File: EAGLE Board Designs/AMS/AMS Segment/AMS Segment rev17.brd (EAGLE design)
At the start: 275.2 x 86 mm, 338 parts, among them J1 CONNECTOR-2_MICROFIT_SMD_RIGH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, J10 CONNECTOR-2_MICROFIT_SMD_RIGH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, J100 CONNECTOR-1_5222_, J101 CONNECTOR-1_5222_, J102 CONNECTOR-1_5222_, J103 CONNECTOR-1_5222_, J104 CONNECTOR-1_5222_, J105 CONNECTOR-1_5222_, J106 CONNECTOR-1_5222_, J107 CONNECTOR-1_5222_, J108 CONNECTOR-1_5222_, J109 CONNECTOR-1_5222_, J110 CONNECTOR-1_5222_, J111 CONNECTOR-1_5222_, J112 CONNECTOR-1_5222_, J113 CONNECTOR-1_5222_, J114 CONNECTOR-1_5222_, J115 CONNECTOR-1_5222_, J116 CONNECTOR-1_5222_, J117 CONNECTOR-1_5222_, J118 CONNECTOR-1_5222_, J119 CONNECTOR-1_5222_, J120 CONNECTOR-1_5222_, J121 CONNECTOR-1_5222_, J2 CONNECTOR-2_MICROFIT_SMD_RIGH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, J3 CONNECTOR-2_MICROFIT_SMD_RIGH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, J4 CONNECTOR-2_MICROFIT_SMD_RIGH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, J5 CONNECTOR-2_MICROFIT_SMD_RIGH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, J6 CONNECTOR-2_MICROFIT_SMD_RIGH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, J7 CONNECTOR-2_MICROFIT_SMD_RIGH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, J8 CONNECTOR-2_MICROFIT_SMD_RIGH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, J9 CONNECTOR-2_MICROFIT_SMD_RIGH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, T1 TRANSFORMER_HM2112ZNLT, U1 LTC6811-2, U2 LTC6811-2, U3 SHT31-ARP-B, U4 SHT31-ARP-B, U5 LT3990-5, U6 LT3990-5

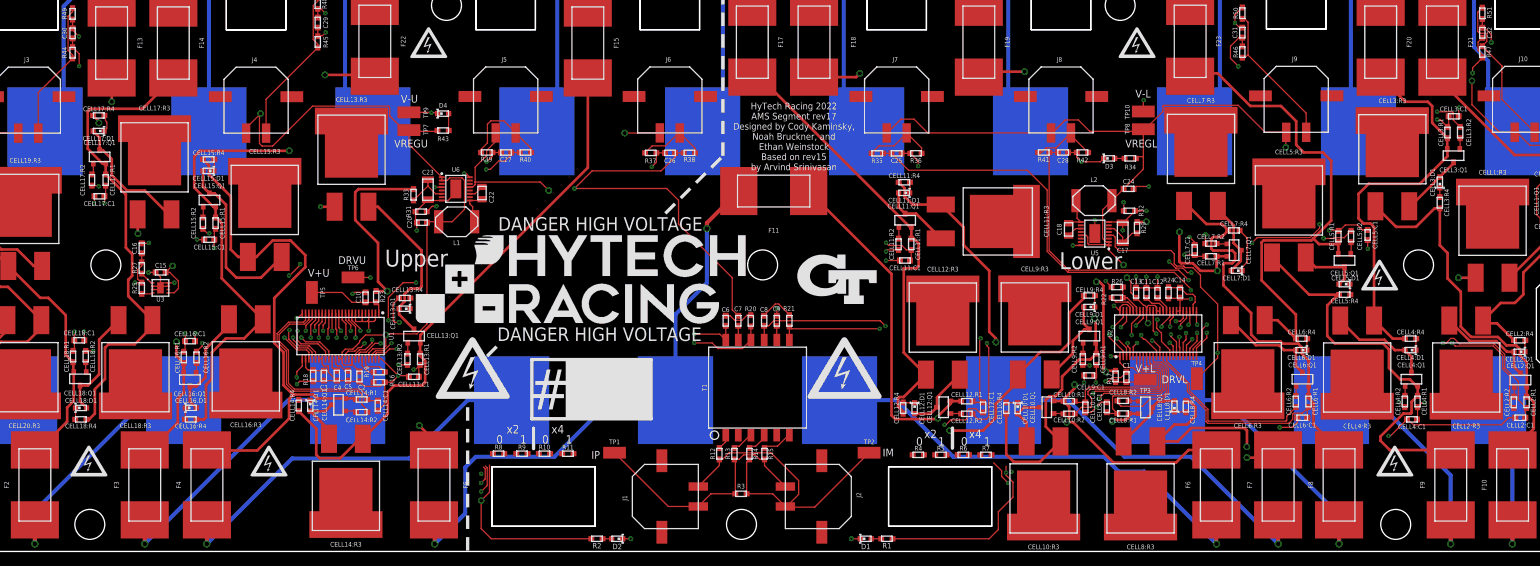
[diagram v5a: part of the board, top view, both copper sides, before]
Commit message: Passes drc and erc
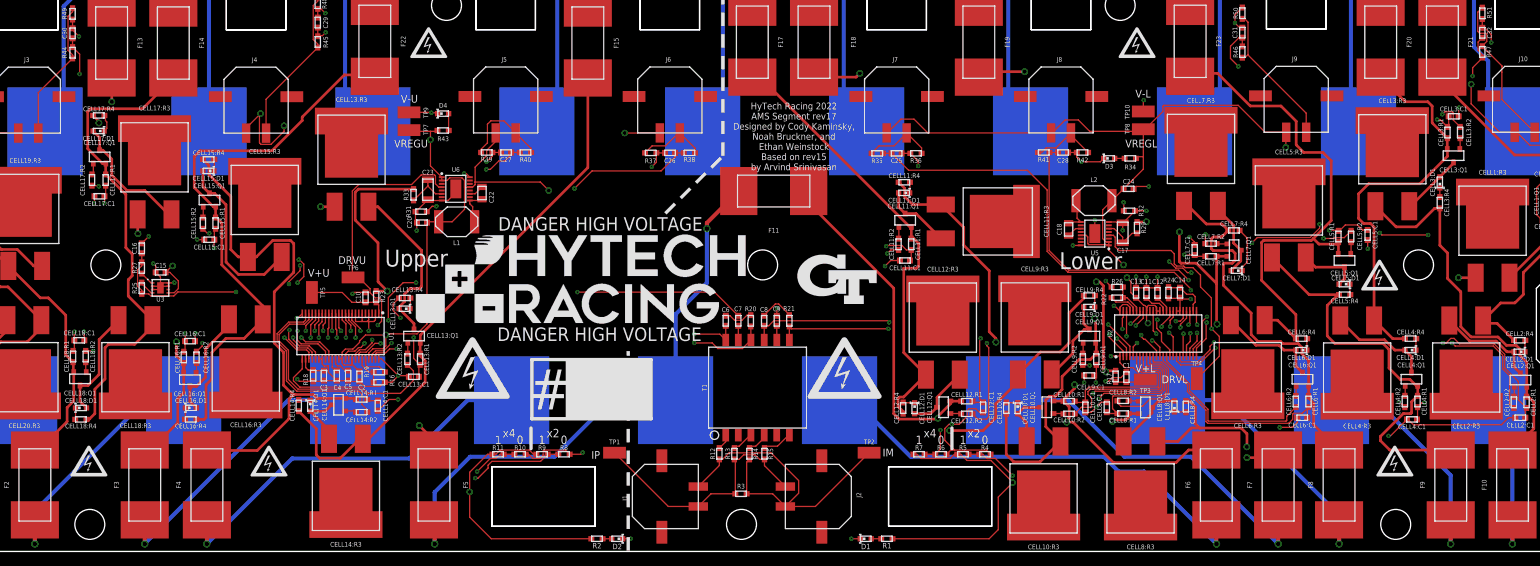
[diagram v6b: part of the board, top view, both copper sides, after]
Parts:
- moved R11 10.5 mm to (100.3, -71.4)
- moved R7 10.1 mm to (163.6, -71.4)
- moved R4 10.0 mm to (173.5, -71.4)
- moved R8 9.83 mm to (110.2, -71.4)
- moved R10 3.68 mm to (103.6, -71.4)
- moved R6 3.37 mm to (166.9, -71.4)
- moved R5 3.32 mm to (170.2, -71.4)
- moved R9 3.02 mm to (106.9, -71.4)
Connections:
- net GPIO5U: now also R25.2; no longer R25.1
- net N$25: now also R8.1; no longer R8.2
- net N$30: now also R25.1; no longer R25.2
- net N$54: now also R10.1; no longer R10.2
- net N$67: now also R4.1, R5.2; no longer R4.2, R5.1
- net N$68: now also R6.1; no longer R6.2
- net V-L: now also R4.2, R6.2; no longer R4.1, R6.1
- net V-U: now also R10.2, R8.2; no longer R10.1, R8.1
- net VREGL: now also R5.1; no longer R5.2
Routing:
- net SENSE7: track 160.0 -> 107.5 mm
- net S3L: track 117.6 -> 66.6 mm
- net S1U: track 72.0 -> 26.2 mm, vias 2 -> 0
- net C3L: track 113.4 -> 67.6 mm
- net GPIO2U: track 85.5 -> 59.9 mm, vias 2 -> 4
- net DRVU: track 71.2 -> 46.8 mm, vias 3 -> 2
- net N$68: track 35.1 -> 53.8 mm
- net C1L: track 93.4 -> 74.8 mm
- net GPIO5U: track 58.3 -> 40.7 mm
- net C2L: track 78.8 -> 64.8 mm
- net S1L: track 83.4 -> 69.7 mm
- net V-L: track 126.7 -> 138.2 mm
- net C11L: track 62.9 -> 51.6 mm
- net S2L: track 73.5 -> 62.2 mm
- net N$25: track 36.2 -> 45.6 mm
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
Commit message: Renumbered
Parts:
- C1: value CAPACITOR_0603_100V_0.1UF -> CAPACITOR_0603_10V_0.1UF
- C11: value CAPACITOR_0603_10V_1UF -> CAPACITOR_1206_100V_2.2UF; device HyTechDevices:0603-CAP -> HyTechDevices:1206-CAP
- C12: value CAPACITOR_0603_10V_1UF -> CAPACITOR_0805_100V_0.22UF; device HyTechDevices:0603-CAP -> HyTechDevices:0805-CAP
- C13, C20, C4, C5: value CAPACITOR_0603_10V_1UF -> CAPACITOR_0603_100V_10NF
- C15: value CAPACITOR_0603_10V_0.1UF -> CAPACITOR_0603_10V_10NF
- C16: value CAPACITOR_0603_10V_3.3NF -> CAPACITOR_0603_10V_15PF
- C17: value CAPACITOR_1206_100V_2.2UF -> CAPACITOR_0603_10V_10NF; device HyTechDevices:1206-CAP -> HyTechDevices:0603-CAP
- C18: value CAPACITOR_0805_100V_0.22UF -> CAPACITOR_0603_10V_15PF; device HyTechDevices:0805-CAP -> HyTechDevices:0603-CAP
- C19: value CAPACITOR_0603_10V_0.1UF -> CAPACITOR_0603_100V_10NF
- C2: value CAPACITOR_0603_10V_22UF -> CAPACITOR_0603_10V_3.3NF
- C21: value CAPACITOR_0603_10V_3.3NF -> CAPACITOR_0805_100V_0.22UF; device HyTechDevices:0603-CAP -> HyTechDevices:0805-CAP
- C22: value CAPACITOR_0805_100V_0.22UF -> CAPACITOR_1206_100V_2.2UF; device HyTechDevices:0805-CAP -> HyTechDevices:1206-CAP
- C23: value CAPACITOR_1206_100V_2.2UF -> CAPACITOR_0603_10V_1UF; device HyTechDevices:1206-CAP -> HyTechDevices:0603-CAP
- C24: value CAPACITOR_0603_10V_22UF -> CAPACITOR_0603_100V_0.1UF
- C25: value CAPACITOR_0603_100V_10NF -> CAPACITOR_0603_10V_22UF
- C26, C27: value CAPACITOR_0603_100V_10NF -> CAPACITOR_0603_10V_1UF
- C30: value CAPACITOR_0603_100V_10NF -> CAPACITOR_0603_10V_0.1UF
- C31: value CAPACITOR_0603_100V_10NF -> CAPACITOR_0603_10V_3.3NF
- C6, C8: value CAPACITOR_0603_10V_15PF -> CAPACITOR_0603_10V_1UF
- C7: value CAPACITOR_0603_10V_10NF -> CAPACITOR_0603_10V_1UF
- C9: value CAPACITOR_0603_10V_10NF -> CAPACITOR_0603_10V_22UF
- R1, R22: value RESISTOR_0603_1K -> RESISTOR_0603_100
- R10: value RESISTOR_0603_DNP -> RESISTOR_0603_374K
- R11, R9: value RESISTOR_0603_DNP -> RESISTOR_0603_1K
- R12: value RESISTOR_0603_22 -> RESISTOR_0603_1K
- R13, R15: value RESISTOR_0603_22 -> RESISTOR_0603_100
- R14: value RESISTOR_0603_22 -> RESISTOR_0603_2.74K
- R16, R19, R2, R34: value RESISTOR_0603_1K -> RESISTOR_0603_DNP
- R17, R18, R37: value RESISTOR_0603_100 -> RESISTOR_0603_DNP
- R20: value RESISTOR_0603_402 -> RESISTOR_0603_2.74K
- R21: value RESISTOR_0603_402 -> RESISTOR_0603_1K
- R23, R25: value RESISTOR_0603_100 -> RESISTOR_0603_402
- R24: value RESISTOR_0603_100 -> RESISTOR_0603_22
- R26: value RESISTOR_0603_1K -> RESISTOR_0603_22
- R28: value RESISTOR_0603_DNP -> RESISTOR_0603_22
- R29: value RESISTOR_0603_470 -> RESISTOR_0603_22
- R3, R5: value RESISTOR_0603_DNP -> RESISTOR_0603_2.74K
- R30, R45: value RESISTOR_0603_100 -> RESISTOR_0603_2.74K
- R31: value RESISTOR_0603_374K -> RESISTOR_0603_100
- R32: value RESISTOR_0603_374K -> RESISTOR_0603_1K
- R33: value RESISTOR_0603_470 -> RESISTOR_0603_DNP
- R36, R48: value RESISTOR_0603_2.74K -> RESISTOR_0603_DNP
- R39, R42: value RESISTOR_0603_2.74K -> RESISTOR_0603_1K
- R4, R6, R7: value RESISTOR_0603_DNP -> RESISTOR_0603_100
- R40: value RESISTOR_0603_100 -> RESISTOR_0603_374K
- R41: value RESISTOR_0603_100 -> RESISTOR_0603_470
- R49, R51: value RESISTOR_0603_2.74K -> RESISTOR_0603_100
- R8: value RESISTOR_0603_DNP -> RESISTOR_0603_470
- U$1, U$23, U$25: device HyTechDevices:MOUNTING_M4 -> HyTechAesthetics:HV_0.50"
- U$10: device HyTechAesthetics:DANGER_HIGH_VOLTAGE -> HyTechAesthetics:LOGO_GT_MEDIUM
- U$100, U$104: device HyTechAesthetics:HV_LARGE -> HyTechAesthetics:HV_0.50"
- U$102, U$103: device HyTechAesthetics:HV_0.50" -> HyTechAesthetics:HV_LARGE
- U$11: device HyTechAesthetics:LOGO_HYTECH_LARGE -> HyTechDevices:MOUNTING_M4
- U$12: device HyTechAesthetics:LOGO_GT_MEDIUM -> HyTechDevices:MOUNTING_M4
- U$13: device HyTechAesthetics:HV_0.50" -> HyTechAesthetics:DANGER_HIGH_VOLTAGE
- U$14: device HyTechDevices:MOUNTING_M4 -> HyTechAesthetics:DANGER_HIGH_VOLTAGE
- U$15: device HyTechDevices:MOUNTING_M4 -> HyTechAesthetics:NUMBER
- U$16: device HyTechDevices:MOUNTING_M4 -> HyTechAesthetics:HV_1.00"
- U$17: device HyTechAesthetics:DANGER_HIGH_VOLTAGE -> HyTechDevices:MOUNTING_M4
- U$19: device HyTechAesthetics:HV_0.50" -> HyTechAesthetics:LOGO_HYTECH_LARGE
- U$21, U$4: device HyTechAesthetics:HV_0.50" -> HyTechDevices:MOUNTING_M4
- U$7: device HyTechAesthetics:NUMBER -> HyTechAesthetics:HV_0.50"
- U$8: device HyTechAesthetics:HV_1.00" -> HyTechDevices:MOUNTING_M4
- U1: value LTC6811-2 -> SHT31-ARP-B; device HyTechDevices:SSOP-48 -> HyTechDevices:DFN-8
- U3, U4: value SHT31-ARP-B -> LT3990-5; device HyTechDevices:DFN-8 -> HyTechDevices:MSOP-16(MSE)
- U5: value LT3990-5 -> LTC6811-2; device HyTechDevices:MSOP-16(MSE) -> HyTechDevices:SSOP-48
- U6: value LT3990-5 -> SHT31-ARP-B; device HyTechDevices:MSOP-16(MSE) -> HyTechDevices:DFN-8
- moved F1 253.8 mm to (268.8, -19.1), turned to 270 degrees
- moved U$25 245.1 mm to (18.4, -9.53)
- moved U$1 243.5 mm to (270.3, -5.71)
- moved U$21 231.9 mm to (41.4, -42.9)
- moved J10 224.8 mm to (29.7, -17.7)
- moved F2 222.0 mm to (252.8, -76.0)
- moved F21 221.7 mm to (30.7, -76.0), turned to 90 degrees
- moved R51 211.9 mm to (36.4, -11.0), turned to 270 degrees
- moved C32 211.8 mm to (36.4, -8.13)
- moved F4 197.2 mm to (242.2, -9.46), turned to 270 degrees
- moved U$4 196.6 mm to (235.2, -81.9)
- moved F3 196.2 mm to (243.5, -76.0)
- moved F23 194.6 mm to (9.75, -9.47)
- moved U1 194.2 mm to (270.3, -39.6), turned to 0 degrees
- moved U$100 193.9 mm to (248.9, -44.5)
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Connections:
- net C0L: now also C5.1, R7.2; no longer C14.1, R24.2
- net C0U: now also C28.1, R47.2, U5.26; no longer C3.1, R18.2, U1.26
- net C1U: now also U5.24; no longer U1.24
- net C2U: now also U5.22; no longer U1.22
- net C3U: now also U5.20; no longer U1.20
- net C4U: now also U5.18; no longer U1.18
- net C5U: now also U5.16; no longer U1.16
- net C6U: now also U5.14; no longer U1.14
- net C7U: now also U5.12; no longer U1.12
- net C8U: now also U5.10; no longer U1.10
- net C9U: now also U5.2, U5.4, U5.6, U5.8; no longer U1.2, U1.4, U1.6, U1.8
- net CC0: now also F1.1; no longer F12.1
- net CC1: now also F4.1; no longer F21.1
- net CC10: now also F8.1, J110.1; no longer F6.1, J116.1
- net CC11: now also F13.1, J111.1; no longer F17.1, J106.1
- net CC12: now also F12.1, F15.1, J112.1; no longer F11.1, F5.1, J117.1
- net CC13: now also F14.1, J113.1; no longer F15.1, J107.1
- net CC14: now also F17.1, J114.1; no longer F4.1, J118.1
- net CC15: now also F16.1, J115.1; no longer F22.1, J108.1
- net CC16: now also F19.1, J116.1; no longer F3.1, J119.1
- net CC17: now also F18.1, J117.1; no longer F14.1, J109.1
- net CC18: now also F21.1, J118.1; no longer F2.1, J120.1
- net CC19: now also F20.1, J119.1; no longer F13.1, J110.1
- net CC2: now also F2.1, J102.1; no longer F10.1, J112.1
- net CC20: now also F22.1, J120.1; no longer F1.1, J121.1
- net CC21: now also F23.1, J121.1; no longer F16.1, J111.1
- net CC3: now also F5.1, J103.1; no longer F20.1, J102.1
- net CC4: now also F3.1, J104.1; no longer F9.1, J113.1
- net CC5: now also F9.1, J105.1; no longer F23.1, J103.1
- net CC6: now also F6.1, J106.1; no longer F8.1, J114.1
- net CC7: now also F10.1, J107.1; no longer F19.1, J104.1
- net CC8: now also J108.1; no longer J115.1
- net CC9: now also F11.1, J109.1; no longer F18.1, J105.1
- net DRVL: now also TP1.1, U3.4; no longer TP4.1, U5.4
- net DRVU: now also TP9.1, U4.4, U5.38; no longer TP6.1, U1.38, U6.4
- net GPIO1L: now also C14.1, R22.2; no longer C25.1, R35.2
- net GPIO1U: now also C32.2, R51.1, U5.27; no longer C30.2, R44.1, U1.27
- net GPIO2L: now also C13.1, R15.2; no longer C28.1, R41.2
- net GPIO2U: now also R46.2, U5.28; no longer R45.2, U1.28
- net GPIO3L: now also C4.1, R6.2; no longer C31.1, R46.2
- net GPIO3U: now also C20.1, R35.2, U5.29; no longer C27.1, R40.2, U1.29
- net GPIO4L: now also C3.2, R4.2; no longer C32.2, R47.2
- net GPIO4U: now also C19.1, R31.2, U5.32; no longer C26.1, R37.2, U1.32
- net GPIO5L: now also C2.1, R1.1, R2.1; no longer C21.1, R28.1, R30.1
- net GPIO5U: now also C31.1, R48.1, R49.2, U5.33; no longer C16.1, R25.2, R27.1, U1.33
- net IM: now also J5.2, J7.2, R26.1, R27.1, R29.1, TP5.1; no longer J1.2, J2.2, R12.1, R14.1, R3.1, TP2.1
- net IML: now also C16.2; no longer C8.2
- net IMU: now also C18.2, U5.41; no longer C6.2, U1.41
- net IP: now also J5.1, J7.1, R24.1, R27.2, R28.1, TP6.1; no longer J1.1, J2.1, R13.1, R15.1, R3.2, TP1.1
- net IPL: now also R23.2; no longer R21.2
- net IPU: now also R25.2, U5.42; no longer R20.2, U1.42
- net N$1: now also R40.2, U4.16; no longer R31.2, U6.16
- net N$10: now also C12.2, L1.1, U3.9; no longer C18.2, L2.1, U5.9
- net N$11: now also C12.1, U3.11; no longer C18.1, U5.11
- net N$12: now also R48.2, U6.1; no longer R27.2, U3.1
- net N$18: now also C17.2; no longer C7.2
- net N$2: now also D1.2, R9.1; no longer D3.2, R34.1
- net N$22: now also R29.2; no longer R12.2
- net N$25: now also R33.1, R34.2, U5.46; no longer R8.1, R9.2, U1.46
- net N$27: now also R28.2; no longer R13.2
- net N$29: now also C15.2; no longer C9.2
- net N$3: now also C21.2, L2.1, U4.9; no longer C22.2, L1.1, U6.9
- net N$30: now also R49.1, U6.4; no longer R25.1, U3.4
- net N$32: now also R26.2; no longer R14.2
- net N$33: now also R24.2; no longer R15.2
- net N$4: now also C21.1, U4.11; no longer C22.1, U6.11
- net N$5: now also D3.2, R32.1; no longer D2.2, R2.1
- net N$54: now also R36.1, R37.2, U5.47; no longer R10.1, R11.2, U1.47
- net N$6: now also D2.2, R21.1; no longer D1.2, R1.1
- net N$61: now also R42.2, R43.2, U5.43; no longer R16.2, R19.2, U1.43
- net N$67: now also R16.1, R17.2; no longer R4.1, R5.2
- net N$68: now also R18.1, R19.2; no longer R6.1, R7.2
- net N$7: now also R10.2, U3.16; no longer R32.2, U5.16
- net N$70: now also R42.1, U5.44; no longer R19.1, U1.44
- net N$71: now also J10.2, R50.1, R51.2; no longer J3.2, R44.2, R49.1
- net N$72: now also R11.2, R12.1; no longer R22.1, R26.2
- net N$73: now also R12.2; no longer R22.2
- net N$76: now also J9.2, R46.1; no longer J4.2, R48.1
- net N$78: now also J8.2, R35.1, R38.1; no longer J5.2, R39.1, R40.1
- net N$80: now also R30.1, R31.1; no longer R37.1, R38.1
- net N$81: now also R1.2, U1.1; no longer R30.2, U4.1
- net N$83: now also R2.2, U1.4; no longer R28.2, U4.4
- net N$84: now also J4.2, R20.1, R22.1; no longer J7.2, R35.1, R36.1
- net N$86: now also J3.2, R14.1, R15.1; no longer J8.2, R41.1, R42.1
- net N$88: now also J2.2, R5.1, R6.1; no longer J9.2, R46.1, R50.1
- net N$9: now also R39.1; no longer R43.1
- net N$90: now also J1.2, R3.2, R4.1; no longer J10.2, R47.1, R51.2
- net N$97: now also C18.1, R25.1; no longer C6.1, R20.1
- net N$99: now also C16.1, R23.1; no longer C8.1, R21.1
- net S1U: now also U5.25; no longer U1.25
- net S2U: now also U5.23; no longer U1.23
- net S3U: now also U5.21; no longer U1.21
- net S4U: now also U5.19; no longer U1.19
- net S5U: now also U5.17; no longer U1.17
- net S6U: now also U5.15; no longer U1.15
- net S7U: now also U5.13; no longer U1.13
- net S8U: now also U5.11; no longer U1.11
- net S9U: now also U5.9; no longer U1.9
- net SENSE1: now also F4.2; no longer F21.2
- net SENSE10: now also F8.2; no longer F6.2
- net SENSE11: now also F13.2; no longer F17.2
- net SENSE12: now also F12.2, R13.2, R8.1; no longer F11.2, R17.2, R29.1
- net SENSE13: now also F14.2; no longer F15.2
- net SENSE14: now also F17.2; no longer F4.2
- net SENSE15: now also F16.2; no longer F22.2
- net SENSE16: now also F19.2; no longer F3.2
- net SENSE17: now also F18.2; no longer F14.2
- net SENSE18: now also F21.2; no longer F2.2
- net SENSE19: now also F20.2; no longer F13.2
- net SENSE2: now also F2.2; no longer F10.2
- net SENSE20: now also F22.2; no longer F1.2
- net SENSE21: now also F23.2, R41.1, R44.1; no longer F16.2, R23.1, R33.1
- net SENSE3: now also F5.2; no longer F20.2
- net SENSE4: now also F3.2; no longer F9.2
- net SENSE5: now also F9.2; no longer F23.2
- net SENSE6: now also F6.2; no longer F8.2
- net SENSE7: now also F10.2; no longer F19.2
- net SENSE9: now also F11.2; no longer F18.2
- net V+L: now also C10.1, R13.1, TP2.1; no longer C1.1, R17.1, TP3.1
- net V+U: now also C24.1, R44.2, TP10.1, U5.1; no longer C10.1, R23.2, TP5.1, U1.1
- net V-L: now also C10.2, C15.1, C2.2, C3.1, C4.2, C5.2, C6.2, C7.2, C8.2, C9.2, D2.1, F1.2, R10.1, R11.1, R14.2, R16.2, R18.2, R20.2, R3.1, R5.2, R7.1, TP3.1, U1.2, U1.3, U1.7, U1.8, U1.PAD, U3.17, U3.8; no longer C12.2, C17.2, C19.2, C21.2, C24.2, C25.2, C28.2, C31.2, C32.1, C9.1, D3.1, F12.2, R24.1, R26.1, R32.1, R36.2, R4.2, R42.2, R50.2, R51.1, R6.2, TP10.1, U4.2, U4.3, U4.7, U4.8, U4.PAD, U5.17, U5.8
- net V-U: now also C17.1, C19.2, C22.2, C24.2, C25.2, C28.2, C30.2, C31.2, C32.1, D3.1, F15.2, R30.2, R33.2, R36.2, R40.1, R43.1, R45.2, R47.1, R50.2, TP7.1, U4.17, U4.8, U5.30, U5.31, U5.48, U6.2, U6.3, U6.7, U6.PAD; no longer C10.2, C15.2, C16.2, C2.2, C3.2, C30.1, C4.2, C5.2, C7.1, D2.1, F5.2, R10.2, R16.1, R18.1, R31.1, R39.2, R48.2, R49.2, R8.2, TP9.1, U1.30, U1.31, U1.48, U3.2, U3.3, U3.7, U3.8, U3.PAD, U6.17
- net VINL: now also C11.1, R8.2, U3.6; no longer C17.1, R29.2, U5.6
- net VINU: now also C22.1, R41.2, U4.6; no longer C23.1, R33.2, U6.6
- net VREF1L: now also C7.1; no longer C11.1
- net VREF1U: now also C26.1, U5.35; no longer C5.1, U1.35
- net VREF2L: now also C6.1; no longer C12.1
- net VREF2U: now also C27.1, U5.34; no longer C4.1, U1.34
- net VREGL: now also C1.1, C8.1, C9.1, J1.1, J2.1, J3.1, J4.1, L1.2, R17.1, R19.1, R21.2, R9.2, TP4.1, U1.5, U3.1, U3.13, U3.2; no longer C13.1, C19.1, C24.1, J10.1, J7.1, J8.1, J9.1, L2.2, R1.2, R34.2, R5.1, R7.1, TP8.1, U4.5, U5.1, U5.13, U5.2
- net VREGU: now also C23.1, C25.1, C30.1, J10.1, J8.1, J9.1, L2.2, R32.2, R34.1, R37.1, R39.2, TP8.1, U4.1, U4.13, U4.2, U5.36, U5.37, U5.40, U5.45, U6.5; no longer C15.1, C2.1, C20.1, J3.1, J4.1, J5.1, L1.2, R11.1, R2.2, R43.2, R9.1, TP7.1, U1.36, U1.37, U1.40, U1.45, U3.5, U6.1, U6.13, U6.2
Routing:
- net N$68: track 53.8 -> 47.5 mm
- net SENSE8: track 102.3 -> 101.2 mm
- net N$67: track 42.3 -> 41.8 mm

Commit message: Final touches
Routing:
- net SENSE8: track 101.2 -> 86.9 mm
- net SENSE9: track 98.7 -> 98.1 mm
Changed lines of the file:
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@@
 <layer number="13" name="Route13" color="21" fill="1" visible="no" active="no"/>
 <layer number="14" name="Route14" color="22" fill="1" visible="no" active="no"/>
-<layer number="15" name="Route15" color="23" fill="1" visible="no" active="yes"/>
-<layer number="16" name="Bottom" color="1" fill="1" visible="no" active="yes"/>
+<layer number="15" name="Route15" color="23" fill="1" visible="yes" active="yes"/>
+<layer number="16" name="Bottom" color="1" fill="1" visible="yes" active="yes"/>
 <layer number="17" name="Pads" color="2" fill="1" visible="yes" active="yes"/>
 <layer number="18" name="Vias" color="2" fill="1" visible="yes" active="yes"/>
@@
 <via x="189.992" y="-50.9702" extent="1-16" drill="0.6096"/>
 <via x="154.6858" y="-14.148" extent="1-16" drill="0.6096"/>
-<wire x1="176.6824" y1="-65.2898" x2="176.6824" y2="-71.3994" width="0.4064" layer="1"/>
-<wire x1="176.6824" y1="-71.3994" x2="177.8" y2="-72.517" width="0.4064" layer="1"/>
-<wire x1="177.8" y1="-72.517" x2="181.7624" y2="-72.517" width="0.4064" layer="1"/>
+<wire x1="176.6824" y1="-65.2898" x2="176.6824" y2="-70.358" width="0.4064" layer="1"/>
+<wire x1="176.6824" y1="-70.358" x2="178.8414" y2="-72.517" width="0.4064" layer="1"/>
+<wire x1="178.8414" y1="-72.517" x2="181.7624" y2="-72.517" width="0.4064" layer="1"/>
 <wire x1="181.7624" y1="-72.517" x2="184.8358" y2="-69.4436" width="0.4064" layer="1"/>
 <wire x1="190.2206" y1="-56.2492" x2="189.3262" y2="-57.1436" width="0.4064" layer="1"/>
@@
 <wire x1="195.1092" y1="-65.278" x2="195.0838" y2="-65.2526" width="0.4064" layer="1"/>
 <via x="212.852" y="-71.882" extent="1-16" drill="0.6096"/>
-<via x="168.1863" y="-67.818" extent="1-16" drill="0.6096"/>
+<via x="189.3445" y="-74.1934" extent="1-16" drill="0.6096"/>
 <via x="192.642659375" y="-66.437340625" extent="1-16" drill="0.6096"/>
 <wire x1="186.1312" y1="-54.6646" x2="184.785" y2="-56.0108" width="0.4064" layer="1"/>
@@
 <wire x1="181.8094" y1="-56.0108" x2="178.435" y2="-59.3852" width="0.4064" layer="1"/>
 <wire x1="178.435" y1="-59.3852" x2="178.435" y2="-60.48430625" width="0.4064" layer="1"/>
-<wire x1="178.435" y1="-60.48430625" x2="175.114" y2="-63.80530625" width="0.4064" layer="1"/>
-<wire x1="175.114" y1="-63.80530625" x2="175.114" y2="-65.9066" width="0.4064" layer="1"/>
-<wire x1="168.1863" y1="-67.818" x2="173.2026" y2="-67.818" width="0.4064" layer="1"/>
-<wire x1="175.114" y1="-65.9066" x2="173.2026" y2="-67.818" width="0.4064" layer="1"/>
-<wire x1="198.08731875" y1="-71.882" x2="212.852" y2="-71.882" width="0.6096" layer="15"/>
+<wire x1="175.9268" y1="-62.99250625" x2="178.435" y2="-60.48430625" width="0.4064" layer="1"/>
+<wire x1="189.3445" y1="-74.1934" x2="188.2269" y2="-73.0758" width="0.4064" layer="1"/>
+<wire x1="198.08731875" y1="-71.882" x2="198.0919875" y2="-71.882" width="0.6096" layer="15"/>
+<wire x1="198.0919875" y1="-71.882" x2="212.852" y2="-71.882" width="0.6096" layer="15"/>
 <wire x1="192.642659375" y1="-66.437340625" x2="198.08731875" y2="-71.882" width="0.6096" layer="15"/>
 <wire x1="192.642659375" y1="-66.437340625" x2="192.86565625" y2="-66.21434375" width="0.4064" layer="1"/>
@@
 <wire x1="212.852" y1="-71.882" x2="216.38615625" y2="-71.882" width="0.4064" layer="1"/>
 <wire x1="216.38615625" y1="-71.882" x2="217.53405625" y2="-70.7341" width="0.4064" layer="1"/>
-<wire x1="168.1863" y1="-67.818" x2="170.47459375" y2="-67.818" width="0.6096" layer="15"/>
-<wire x1="170.47459375" y1="-67.818" x2="175.5394" y2="-72.88280625" width="0.6096" layer="15"/>
-<wire x1="175.5394" y1="-72.88280625" x2="175.5394" y2="-74.5154625" width="0.6096" layer="15"/>
-<wire x1="175.5394" y1="-74.5154625" x2="176.4682875" y2="-75.44435" width="0.6096" layer="15"/>
-<wire x1="186.2047875" y1="-71.882" x2="198.08731875" y2="-71.882" width="0.6096" layer="15"/>
-<wire x1="176.4682875" y1="-75.44435" x2="182.6424375" y2="-75.44435" width="0.6096" layer="15"/>
-<wire x1="182.6424375" y1="-75.44435" x2="186.2047875" y2="-71.882" width="0.6096" layer="15"/>
+<wire x1="195.7996375" y1="-74.17435" x2="189.36355" y2="-74.17435" width="0.6096" layer="15"/>
+<wire x1="189.3445" y1="-74.1934" x2="189.36355" y2="-74.17435" width="0.6096" layer="15"/>
+<wire x1="195.7996375" y1="-74.17435" x2="198.0919875" y2="-71.882" width="0.6096" layer="15"/>
+<wire x1="178.48293125" y1="-73.0758" x2="175.9268" y2="-70.51966875" width="0.4064" layer="1"/>
+<wire x1="175.9268" y1="-70.51966875" x2="175.9268" y2="-62.99250625" width="0.4064" layer="1"/>
+<wire x1="188.2269" y1="-73.0758" x2="178.48293125" y2="-73.0758" width="0.4064" layer="1"/>
 </signal>
 <signal name="SENSE7" class="4">
@@
 <signal name="N$67">
 <contactref element="U2" pad="46"/>
-<via x="177.673" y="-73.9902" extent="1-16" drill="0.254"/>
-<wire x1="177.673" y1="-73.9902" x2="175.6854" y2="-72.0026" width="0.1524" layer="1"/>
-<wire x1="175.6854" y1="-72.0026" x2="173.7873125" y2="-72.0026" width="0.1524" layer="1"/>
+<via x="177.6476" y="-73.9902" extent="1-16" drill="0.254"/>
+<wire x1="177.6476" y1="-73.9902" x2="177.5206" y2="-73.9902" width="0.1524" layer="1"/>
+<wire x1="177.5206" y1="-73.9902" x2="175.533" y2="-72.0026" width="0.1524" layer="1"/>
+<wire x1="175.533" y1="-72.0026" x2="173.7873125" y2="-72.0026" width="0.1524" layer="1"/>
 <via x="194.75561875" y="-53.6448" extent="1-16" drill="0.254"/>
 <wire x1="194.31111875" y1="-62.25428125" x2="182.5752" y2="-73.9902" width="0.1524" layer="15"/>
-<wire x1="177.673" y1="-73.9902" x2="182.5752" y2="-73.9902" width="0.1524" layer="15"/>
+<wire x1="177.6476" y1="-73.9902" x2="182.5752" y2="-73.9902" width="0.1524" layer="15"/>
 <wire x1="194.75561875" y1="-53.6448" x2="194.75561875" y2="-54.7116" width="0.1524" layer="15"/>
 <wire x1="194.75561875" y1="-54.7116" x2="194.31111875" y2="-55.1561" width="0.1524" layer="15"/>
